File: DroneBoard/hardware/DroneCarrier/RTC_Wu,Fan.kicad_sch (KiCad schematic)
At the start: 14 parts, among them J2 Molex 470531000, U1 PCF85063AT/AAZ, U2 74LVC1G07SE-7, U3 EMC2301-1-ACZL-TR, Y1 X32K768S301

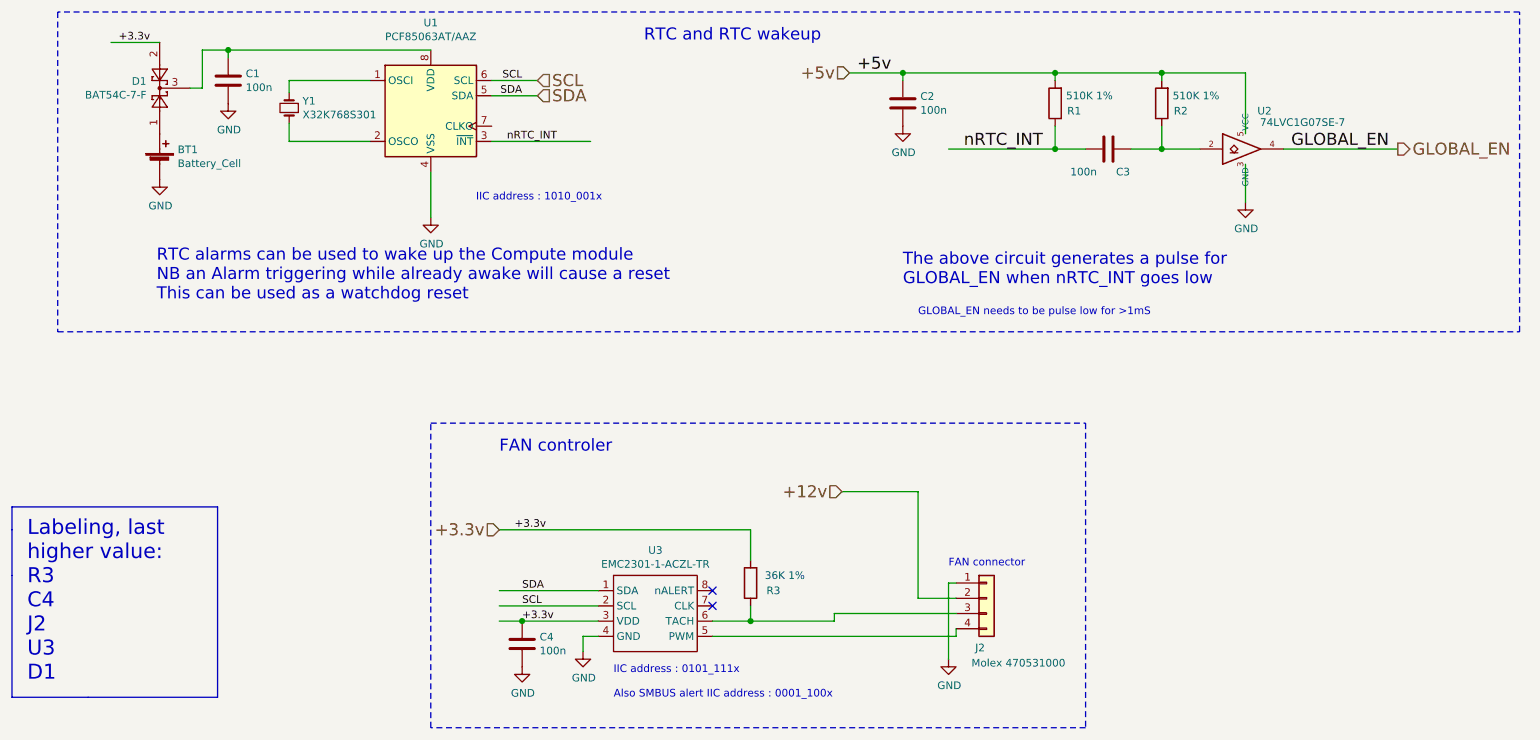
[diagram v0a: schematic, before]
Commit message: Labelling needs to be compared to the RPi CM4
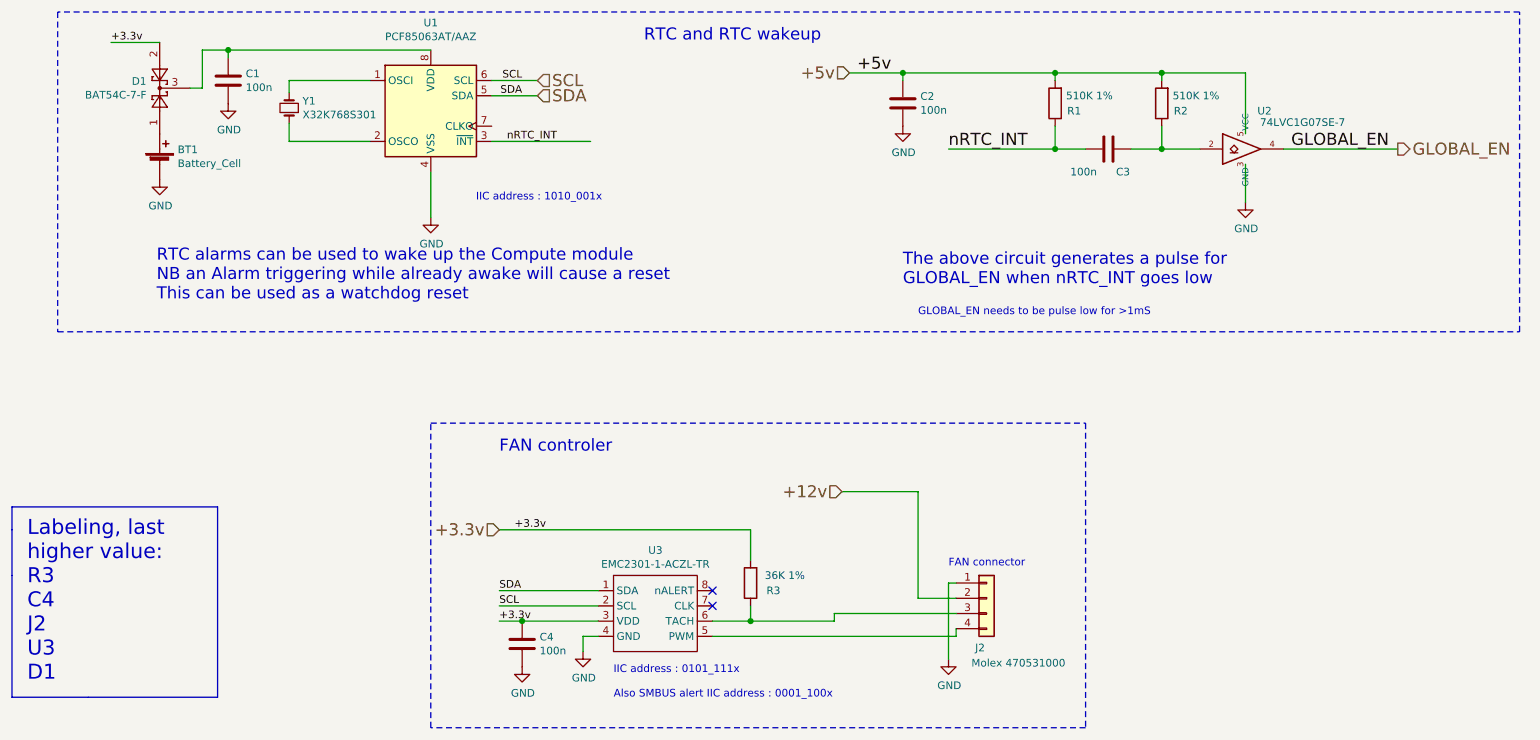
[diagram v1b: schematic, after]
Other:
- company: (none) -> Surveilia
- title: (none) -> RTC
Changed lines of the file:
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@@
 (kicad_sch (version 20210621) (generator eeschema)
   (paper "A4")
+  (title_block
+    (title "RTC")
+    (date "2021-10-22")
+    (rev "01")
+    (company "Surveilia")
+    (comment 1 "Author: Chase W. & Kaden T.")
+  )
   (junction (at 52.578 48.26) (diameter 1.016) (color 0 0 0 0))
   (junction (at 101.6 143.51) (diameter 1.016) (color 0 0 0 0))
@@
     (effects (font (size 1.27 1.27)) (justify left bottom))
   )
-  (label "+3.3v" (at 34.29 46.99 0)
+  (label "+3.3v" (at 33.02 46.99 0)
+    (effects (font (size 1.27 1.27)) (justify left bottom))
+  )
+  (label "SDA" (at 97.79 138.43 0)
+    (effects (font (size 1.27 1.27)) (justify left bottom))
+  )
+  (label "SCL" (at 97.79 140.97 0)
+    (effects (font (size 1.27 1.27)) (justify left bottom))
+  )
+  (label "+3.3v" (at 97.79 143.51 0)
     (effects (font (size 1.27 1.27)) (justify left bottom))
   )
@@
     (effects (font (size 1.27 1.27)) (justify right bottom))
   )
-  (label "SDA" (at 101.6 138.43 0)
-    (effects (font (size 1.27 1.27)) (justify left bottom))
-  )
-  (label "SCL" (at 101.6 140.97 0)
-    (effects (font (size 1.27 1.27)) (justify left bottom))
-  )
-  (label "+3.3v" (at 101.6 143.51 0)
-    (effects (font (size 1.27 1.27)) (justify left bottom))
-  )
   (label "+5v" (at 157.48 52.07 0)
     (effects (font (size 2.0066 2.0066)) (justify left bottom))
   )
-  (label "nRTC_INT" (at 175.26 64.77 0)
+  (label "nRTC_INT" (at 172.72 64.77 0)
     (effects (font (size 2.0066 2.0066)) (justify left bottom))
   )
@@
   (symbol (lib_id "power:GND") (at 41.148 69.85 0) (unit 1)
     (in_bom yes) (on_board yes)
-    (property "Reference" "#PWR?" (id 0) (at 41.148 76.2 0)
+    (property "Reference" "#PWR0127" (id 0) (at 41.148 76.2 0)
       (effects (font (size 1.27 1.27)) hide)
     )
@@
   (symbol (lib_id "power:GND") (at 52.578 57.1754 0) (unit 1)
     (in_bom yes) (on_board yes)
-    (property "Reference" "#PWR?" (id 0) (at 52.578 63.5254 0)
+    (property "Reference" "#PWR0124" (id 0) (at 52.578 63.5254 0)
       (effects (font (size 1.27 1.27)) hide)
     )
@@
   (symbol (lib_id "power:GND") (at 86.36 76.2 0) (unit 1)
     (in_bom yes) (on_board yes)
-    (property "Reference" "#PWR?" (id 0) (at 86.36 82.55 0)
+    (property "Reference" "#PWR0126" (id 0) (at 86.36 82.55 0)
       (effects (font (size 1.27 1.27)) hide)
     )
@@
   (symbol (lib_id "power:GND") (at 101.6 151.13 0) (unit 1)
     (in_bom yes) (on_board yes)
-    (property "Reference" "#PWR?" (id 0) (at 101.6 157.48 0)
+    (property "Reference" "#PWR0128" (id 0) (at 101.6 157.48 0)
       (effects (font (size 1.27 1.27)) hide)
     )
@@
   (symbol (lib_id "power:GND") (at 111.76 148.59 0) (unit 1)
     (in_bom yes) (on_board yes)
-    (property "Reference" "#PWR?" (id 0) (at 111.76 154.94 0)
+    (property "Reference" "#PWR0129" (id 0) (at 111.76 154.94 0)
       (effects (font (size 1.27 1.27)) hide)
     )
@@
   (symbol (lib_id "power:GND") (at 165.1 60.96 0) (unit 1)
     (in_bom yes) (on_board yes)
-    (property "Reference" "#PWR?" (id 0) (at 165.1 67.31 0)
+    (property "Reference" "#PWR0123" (id 0) (at 165.1 67.31 0)
       (effects (font (size 1.27 1.27)) hide)
     )
@@
   (symbol (lib_id "power:GND") (at 172.72 149.86 0) (unit 1)
     (in_bom yes) (on_board yes)
-    (property "Reference" "#PWR?" (id 0) (at 172.72 156.21 0)
+    (property "Reference" "#PWR0122" (id 0) (at 172.72 156.21 0)
       (effects (font (size 1.27 1.27)) hide)
     )
@@
   (symbol (lib_id "power:GND") (at 222.25 73.66 0) (unit 1)
     (in_bom yes) (on_board yes)
-    (property "Reference" "#PWR?" (id 0) (at 222.25 80.01 0)
-      (effects (font (size 1.27 1.27)) hide)
-    )
+    (property "Reference" "#PWR0125" (id 0) (at 222.25 80.01 0)
+      (effects (font (size 1.27 1.27)) hide)
+    )
